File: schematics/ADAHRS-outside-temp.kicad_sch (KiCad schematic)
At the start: 11 parts, among them U1 Opamp_Dual

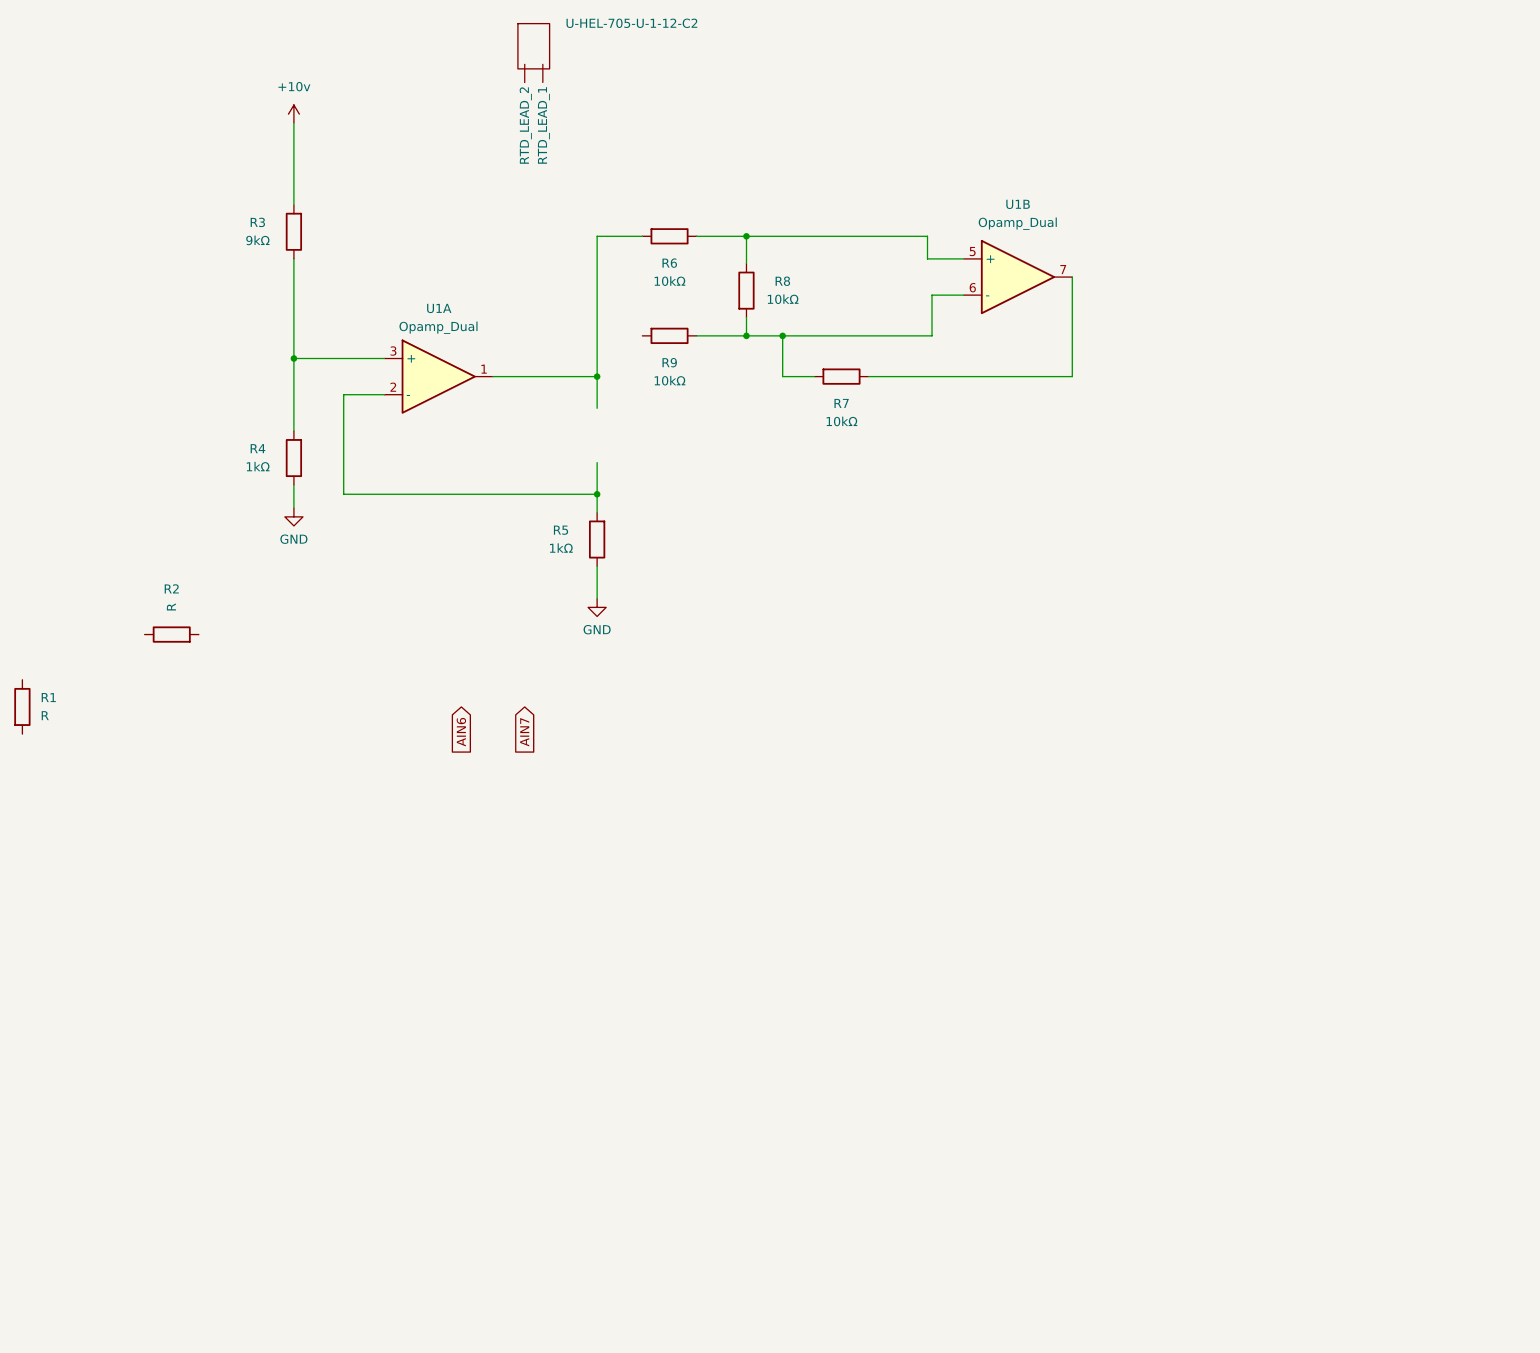
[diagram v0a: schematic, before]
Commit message: outside temp v1_01
will shortcut where I integrated the HEL 705 sensor. I need to fix this.
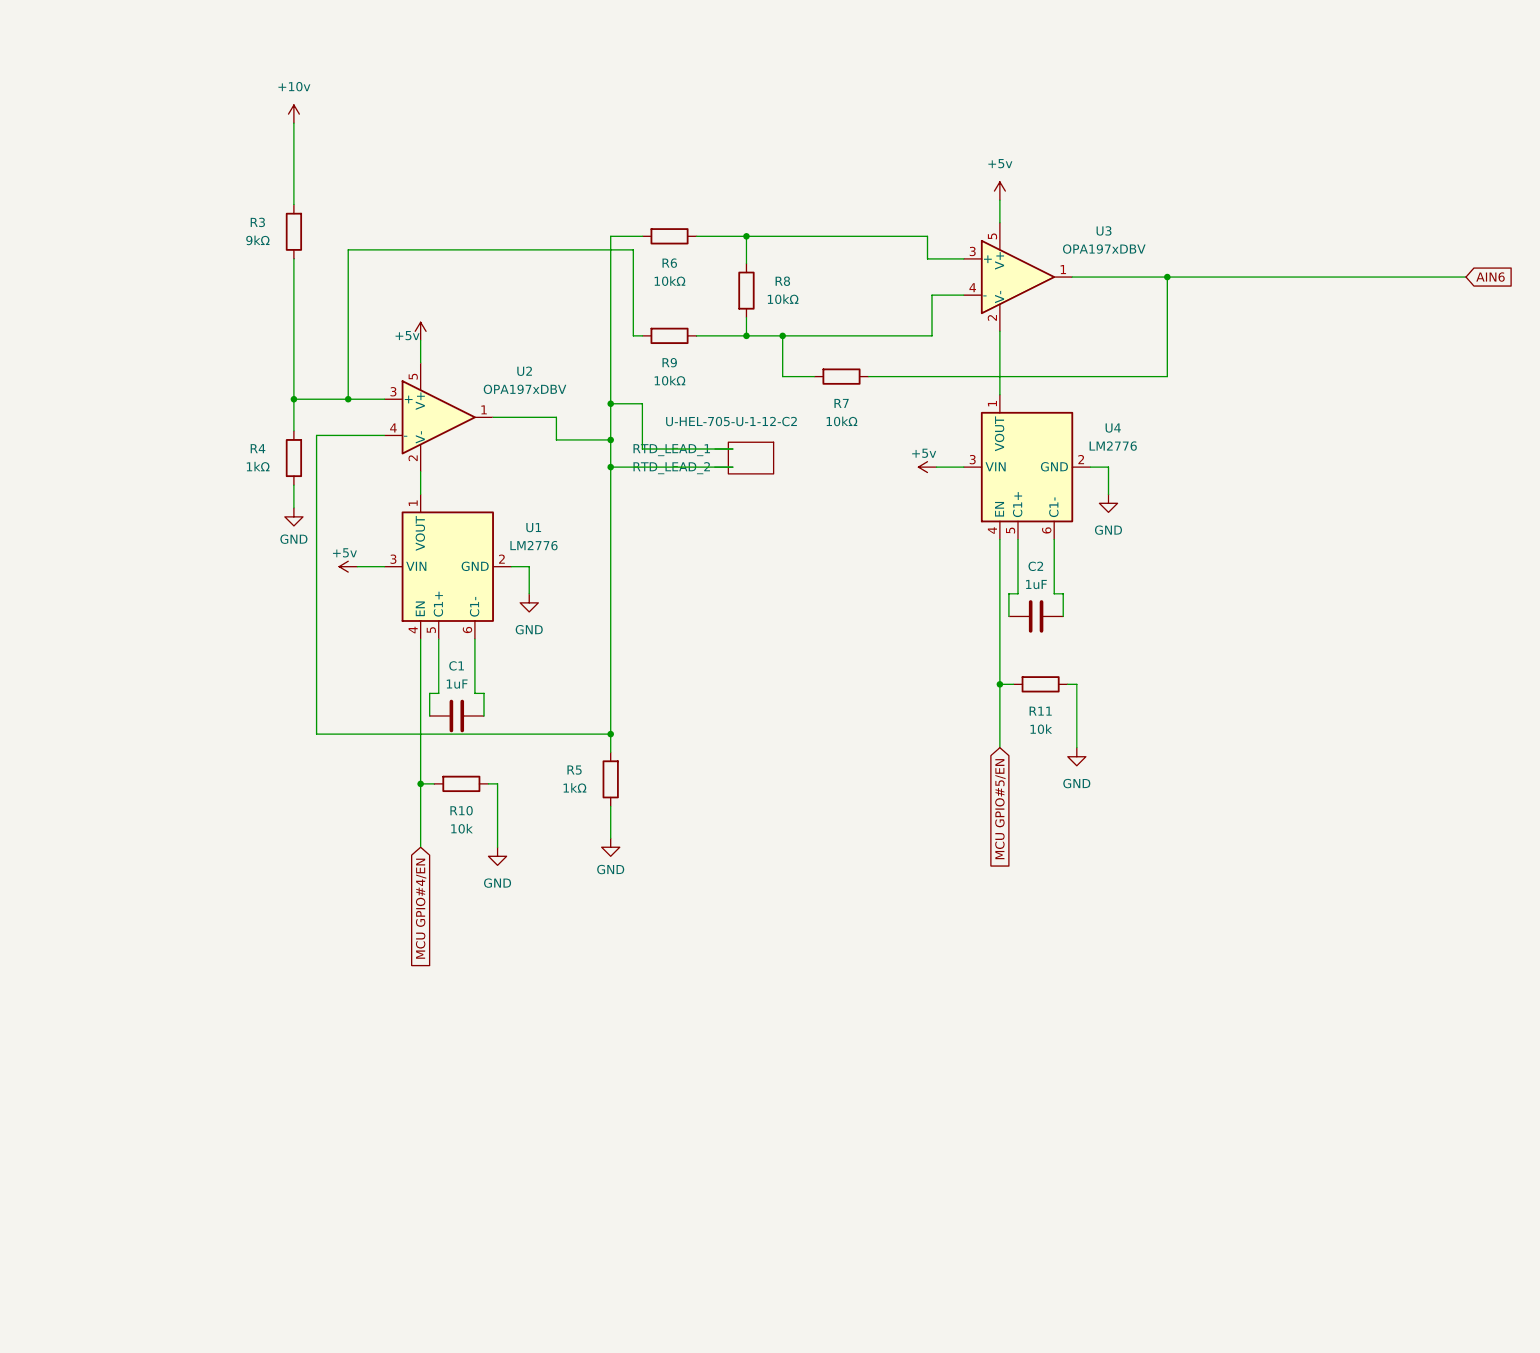
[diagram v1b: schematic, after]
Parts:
- removed R1, R2: R, symbol Device:R
- removed U1: Opamp_Dual, symbol Device:Opamp_Dual
- added C1, C2: 1uF, symbol Device:C
- added R10, R11: 10k, symbol Device:R
- added U1, U4: LM2776, Package_TO_SOT_SMD:SOT-23-6, symbol Regulator_SwitchedCapacitor:LM2776
- added U2, U3: OPA197xDBV, Package_TO_SOT_SMD:SOT-23-5, symbol Amplifier_Operational:OPA197xDBV
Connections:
- net AIN6: now also R7.1, U3.1
- net GND: now also R10.1, R11.1, U1.2 (GND), U4.2 (GND)
- net at R6.1, R8.1: now also U3.3 (+)
- net at R6.2: now also R5.2, U-HEL-705-U-1-12-C2. (RTD_LEAD_2), U2.1, U2.4 (-)
- net at R3.1, R4.2: now also R9.2, U2.3 (+)
- net at R7.2, R8.2, R9.1: now also U3.4 (-)
- new net: C1.1, U1.5 (C1+)
- new net: C1.2, U1.6 (C1-)
- new net: U1.1 (VOUT), U2.2 (V-)
- new net: U3.2 (V-), U4.1 (VOUT)
- new net: C2.1, U4.5 (C1+)
- new net: C2.2, U4.6 (C1-)
- new net +5v: U1.3 (VIN), U2.5 (V+), U3.5 (V+), U4.3 (VIN)
- new net MCU GPIO#4/EN: R10.2, U1.4 (EN)
- new net MCU GPIO#5/EN: R11.2, U4.4 (EN)
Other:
- moved on the sheet: R5, U-HEL-705-U-1-12-C2

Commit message: Revised draft of temp sensor v1_02
I did the math and double checked the circuit that removed the offset and fixed errors. I have not looked at each component and check if there are actual connections. However, I took to the paper and re wrote the circuit diagram in my notes. I need to photocopy 2 pages of what I did. I gave notes on how the linear voltage output actually worked and functions well making it easier for the ADC to understand.
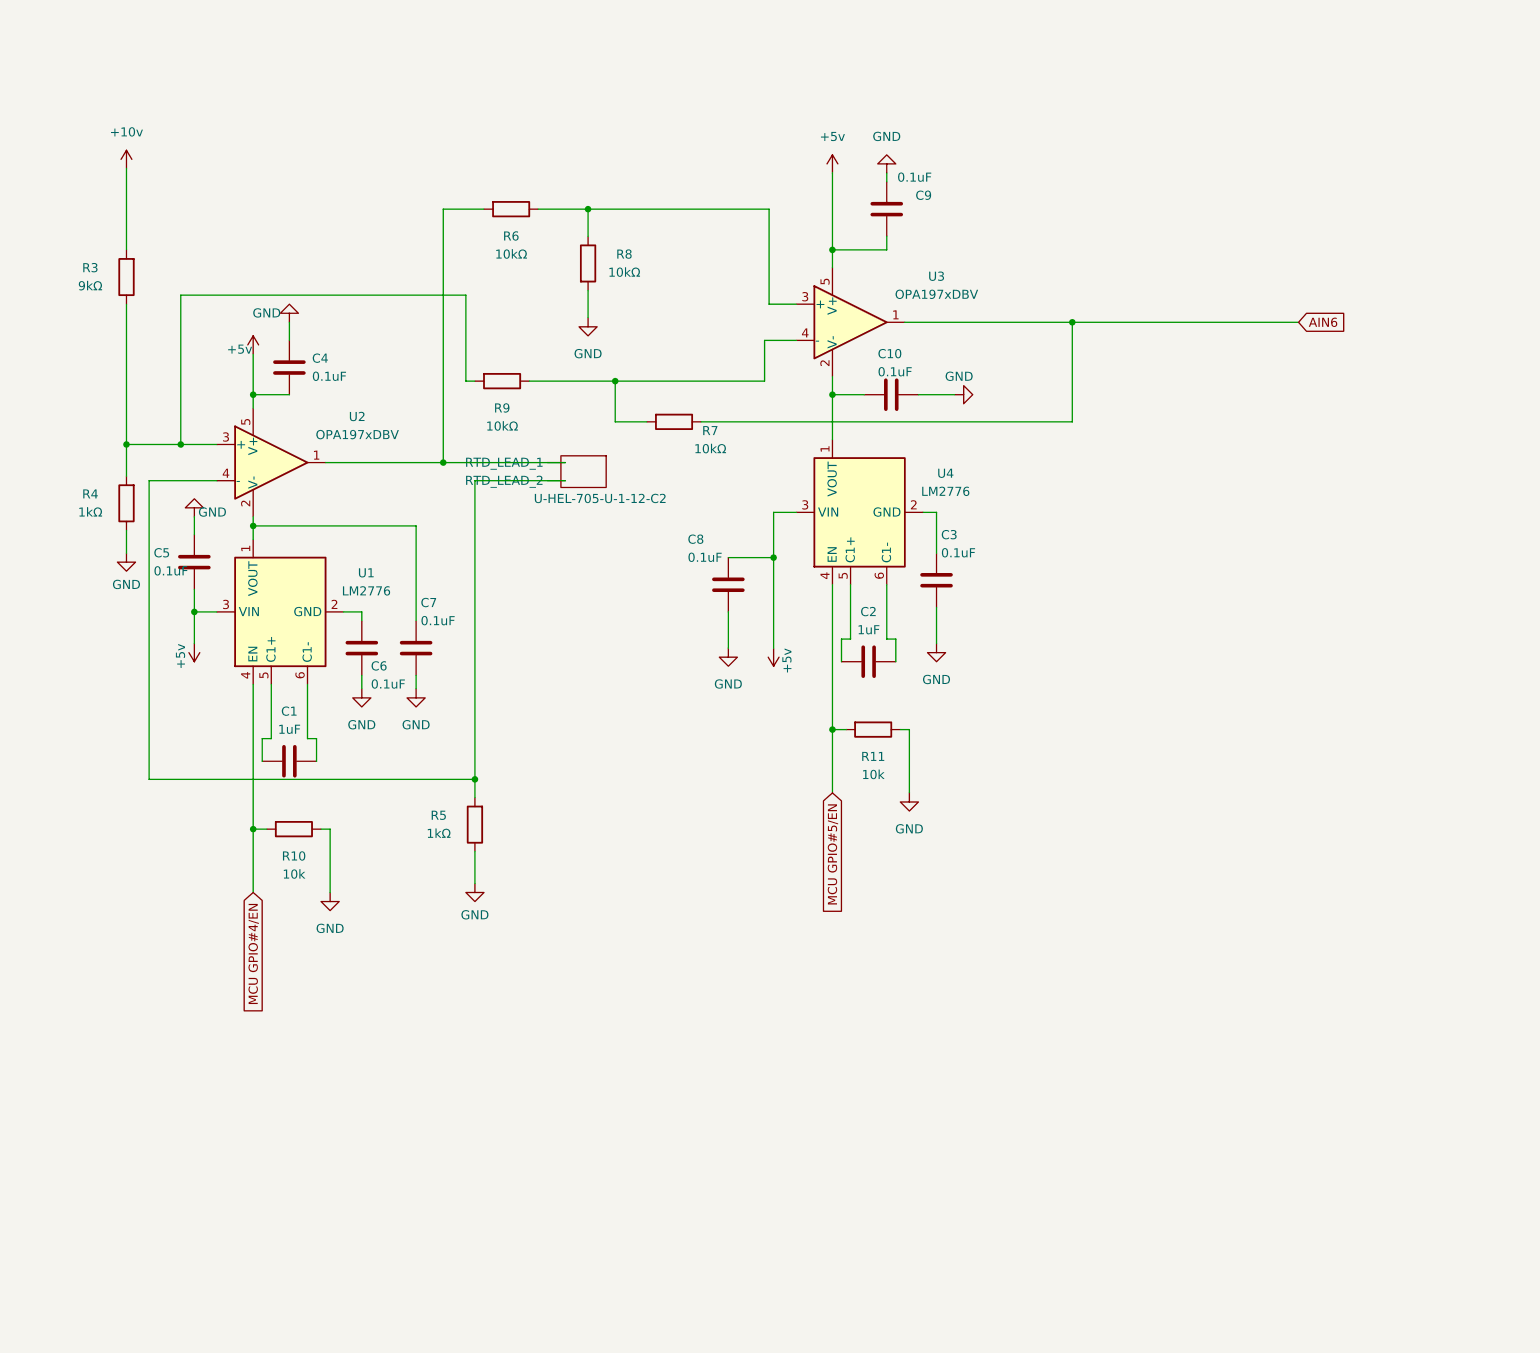
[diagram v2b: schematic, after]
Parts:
- added C10, C3, C4, C5, C6, C7, C8, C9: 0.1uF, symbol Device:C
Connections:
- net +5v: now also C4.1, C5.1, C8.2, C9.2
- net GND: now also R8.2, C10.1, C3.1, C4.2, C5.2, C6.1, C7.1, C8.1, C9.1; no longer U1.2 (GND), U4.2 (GND)
- net at R5.2, U-HEL-705-U-1-12-C2. (RTD_LEAD_2), U2.4 (-): no longer R6.2, U2.1
- net at U1.1 (VOUT), U2.2 (V-): now also C7.2
- net at U3.2 (V-), U4.1 (VOUT): now also C10.2
- net at R7.2, R9.1, U3.4 (-): no longer R8.2
- new net: C6.2, U1.2 (GND)
- new net: R6.2, U-HEL-705-U-1-12-C2. (RTD_LEAD_2), U2.1
- new net: C3.2, U4.2 (GND)
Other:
- moved on the sheet: C1, C2, R10, R11, R3, R4, R5, R6, R7, R8, R9, U-HEL-705-U-1-12-C2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

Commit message: pin header v1.03
I replaced the custom symbol sensor with pin header since the sensor is not going to be inside the lru.
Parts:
- removed U-HEL-705-U-1-12-C2: ~, symbol custom:HEL-705-U-1-12-C2
- added J1: Connector_PinHeader_2.54mm:PinHeader_1x02_P2.54mm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, symbol Connector_Generic:Conn_01x02
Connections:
- net at R6.2, U2.1: now also J1.1 (Pin_1)
- net at R5.2, U2.4 (-): now also J1.2 (Pin_2)
- net MCU GPIO#4/EN renamed MCU NHET0/EN
- net MCU GPIO#5/EN renamed MCU NHET1/EN
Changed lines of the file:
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@@
 	(title_block
 		(title "outside air temperature")
-		(rev "-")
+		(date "09/13/26")
+		(rev "C")
 		(comment 1 "This is the linear output voltage given in the datasheet for this component")
 	)
@@
 		)
 	)
-	(global_label "MCU GPIO#4{slash}EN"
+	(global_label "MCU NHET0{slash}EN"
 		(shape input)
 		(at 92.71 137.16 270)
@@
 		)
 		(property "Intersheetrefs" "${INTERSHEET_REFS}"
-			(at 92.71 155.9295 90)
+			(at 92.71 154.9618 90)
 			(effects
 				(font
@@
 		)
 	)
-	(global_label "MCU GPIO#5{slash}EN"
+	(global_label "MCU NHET1{slash}EN"
 		(shape input)
 		(at 173.99 123.19 270)
@@
 		)
 		(property "Intersheetrefs" "${INTERSHEET_REFS}"
-			(at 173.99 141.9595 90)
+			(at 173.99 140.9918 90)
 			(effects
 				(font
@@
 	)
 	(symbol
+		(lib_id "Connector_Generic:Conn_01x02")
+		(at 141.605 76.835 0)
+		(unit 1)
+		(exclude_from_sim no)
+		(in_bom yes)
+		(on_board yes)
+		(dnp no)
+		(property "Reference" "J1"
+			(at 144.78 76.8349 0)
+			(effects
+				(font
+					(size 1.27 1.27)
+				)
+				(justify left)
+			)
+		)
+		(property "Value" "Connector_PinHeader_2.54mm:PinHeader_1x02_P2.54mm_Vertical"
+			(at 130.81 73.025 0)
+			(effects
+				(font
+					(size 1.27 1.27)
+				)
+				(justify left)
+			)
+		)
+		(property "Footprint" ""
+			(at 141.605 76.835 0)
+			(effects
+				(font
+					(size 1.27 1.27)
+				)
+				(hide yes)
+			)
+		)
+		(property "Datasheet" "~"
+			(at 141.605 76.835 0)
+			(effects
+				(font
+					(size 1.27 1.27)
+				)
+				(hide yes)
+			)
+		)
+		(property "Description" "Generic connector, single row, 01x02, script generated (kicad-library-utils/schlib/autogen/connector/)"
+			(at 141.605 76.835 0)
+			(effects
+				(font
+					(size 1.27 1.27)
+				)
+				(hide yes)
+			)
+		)
+		(pin "1"
+		)
+		(pin "2"
+		)
+		(instances
+			(project ""
+				(path "/1c9d1702-4215-4f0e-92e0-1fbfd28a9266"
+					(reference "J1")
+					(unit 1)
+				)
+			)
+		)
+	)
+	(symbol
 		(lib_id "Device:R")
 		(at 74.93 82.55 180)
@@
 		(dnp no)
 		(property "Reference" "R7"
-			(at 156.845 72.39 90)
+			(at 157.48 67.31 90)
 			(effects
 				(font
@@
 		)
 		(property "Value" "10kΩ"
-			(at 156.845 74.93 90)
+			(at 157.48 69.85 90)
 			(effects
 				(font
@@
 					(unit 1)
 				)
-			)
-		)
-	)
-	(symbol
-		(lib_id "custom:HEL-705-U-1-12-C2")
-		(at 139.065 78.105 270)
-		(unit 1)
-		(exclude_from_sim no)
-		(in_bom yes)
-		(on_board yes)
-		(dnp no)
-		(property "Reference" "U-HEL-705-U-1-12-C2"
-			(at 132.08 81.915 90)
-			(effects
-				(font
-					(size 1.27 1.27)
-				)
-				(justify left)
-			)
-		)
-		(property "Value" "~"
-			(at 136.8425 81.915 0)
-			(effects
-				(font
-					(size 1.27 1.27)
-				)
-				(justify left)
-			)
-		)
-		(property "Footprint" ""
-			(at 139.065 78.105 0)
-			(effects
-				(font
-					(size 1.27 1.27)
-				)
-				(hide yes)
-			)
-		)
-		(property "Datasheet" ""
-			(at 139.065 78.105 0)
-			(effects
-				(font
-					(size 1.27 1.27)
-				)
-				(hide yes)
-			)
-		)
-		(property "Description" ""
-			(at 139.065 78.105 0)
-			(effects
-				(font
-					(size 1.27 1.27)
-				)
-				(hide yes)
-			)
-		)
-		(pin ""
-		)
-		(pin ""
-		)
-		(instances
-			(project ""
-				(path "/1c9d1702-4215-4f0e-92e0-1fbfd28a9266"
-					(reference "U-HEL-705-U-1-12-C2")
-					(unit 1)
-				)
